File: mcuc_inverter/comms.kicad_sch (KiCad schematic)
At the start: 0 parts

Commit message: Capture bus_sense, temp_sense, comms: all 11 sheets now live
bus_sense: 4x750k + 12.0k string (strict series, 124.5 V/part) into
AMC1311BDWV (pinout verified vs SBAS786C; B-grade 3.0-5.5 V VDD1 is
load-bearing per D022; no input clamp diodes per TI 9.3), HV-side
3.3 V from MCP1804T-3302 (2-28 V in, stocked - no TBV needed) off
the VGD_LS rail, diff-to-SE gain 0.75: V_BUS = 2.988 mV/V, 500 V ->
1.494 V, saturates ~1.50 V, always < 3.3 V.

temp_sense: coldplate NTC channel (B57861S off-board via J1101),
board NTC (NCU18 successor), 6x DNP TS provision pads onto the
module TS pins with D022 rationale quoted on-sheet.

comms: ISO1042DWR isolated CAN (VCC2 pins 11/16 tied - datasheet
requirement), split termination + TVS added (legacy sheet flagged
its own missing protection), USB-C + USBLC6 to MCU 70/71, keyed SWD,
status LEDs, I/O connectors. CAN_TX/RX verified onto MCU pins 96/95;
CONTACTOR_P/N resolve onto the precharge coil driver.

ERC 0 errors; netlist machine-checks per sheet; key cross-sheet
nets independently re-verified. 11 of 11 sheets captured.

Co-Authored-By: Claude Fable 5 <noreply@anthropic.com>
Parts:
- added C1201, C1202: 100nF, Capacitor_SMD:C_0603_1608Metric, symbol Device:C
- added C1203: 4.7nF, Capacitor_SMD:C_0603_1608Metric, symbol Device:C
- added C1204: 4.7uF, Capacitor_SMD:C_0805_2012Metric, symbol Device:C
- added D1201: NUP2105L, Package_TO_SOT_SMD:SOT-23, symbol Power_Protection:NUP2105L
- added D1202: GREEN PWR, LED_SMD:LED_0603_1608Metric, symbol Device:LED
- added D1203: RED FAULT, LED_SMD:LED_0603_1608Metric, symbol Device:LED
- added J1201: CAN bus (H/L/GND/nc), Connector_JST:JST_PH_B4B-PH-K_1x04_P2.00mm_Vertical, symbol Connector_Generic:Conn_01x04
- added J1202: GCT USB4085-GF-A, Connector_USB:USB_C_Receptacle_GCT_USB4085, symbol Connector:USB_C_Receptacle_USB2.0_16P
- added J1203: Aux 12-24 V in, Connector_JST:JST_VH_B2P-VH_1x02_P3.96mm_Vertical, symbol Connector_Generic:Conn_01x02
- added J1204: Main contactor coil, Connector_JST:JST_VH_B4P-VH_1x04_P3.96mm_Vertical, symbol Connector_Generic:Conn_01x04
- added J1205: Hall + motor temp, Connector_JST:JST_SH_SM08B-SRSS-TB_1x08-1MP_P1.00mm_Horizontal, symbol Connector_Generic:Conn_01x08
- added J1206: Encoder / SinCos, Connector_JST:JST_SH_SM08B-SRSS-TB_1x08-1MP_P1.00mm_Horizontal, symbol Connector_Generic:Conn_01x08
- added J1207: Resolver, Connector_JST:JST_SH_SM06B-SRSS-TB_1x06-1MP_P1.00mm_Horizontal, symbol Connector_Generic:Conn_01x06
- added J1208: FTSH-105-01-L-DV-K, Connector_PinHeader_1.27mm:PinHeader_2x05_P1.27mm_Vertical_SMD, symbol Connector:Conn_ARM_JTAG_SWD_10
- added R1202, R1203: 60.4R, Resistor_SMD:R_0603_1608Metric, symbol Device:R
- added R1204, R1205: 5.1k, Resistor_SMD:R_0603_1608Metric, symbol Device:R
- added R1206: 47k, Resistor_SMD:R_0603_1608Metric, symbol Device:R
- added R1207: 22k, Resistor_SMD:R_0603_1608Metric, symbol Device:R
- added R1208, R1209: 1k, Resistor_SMD:R_0603_1608Metric, symbol Device:R
- added U1201: ISO1042DWR, Package_SO:SOIC-16W_7.5x10.3mm_P1.27mm, symbol mcuc:ISO1042DWR
- added U1202: USBLC6-2SC6, Package_TO_SOT_SMD:SOT-23-6, symbol Power_Protection:USBLC6-2SC6
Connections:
- new net: D1203.2 (A), R1209.2
- new net: J1202.A6 (D+), J1202.B6 (D+), U1202.3 (I/O2)
- new net: J1202.A7 (D-), J1202.B7 (D-), U1202.1 (I/O1)
- new net: D1202.2 (A), R1208.2
- new net: C1203.1, R1202.2, R1203.1
- new net +3.3V: C1201.1, J1205.1 (Pin_1), J1206.1 (Pin_1), J1208.1 (VTref), R1208.1, R1209.1, U1201.1 (VCC1)
- new net AUX_IN: J1203.1 (Pin_1)
- new net CANH: D1201.1 (K), J1201.1 (Pin_1), R1202.1, U1201.13 (CANH)
- new net CANL: D1201.2 (K), J1201.2 (Pin_2), R1203.2, U1201.12 (CANL)
- new net CAN_5V: C1202.1, C1204.1, U1201.11 (VCC2), U1201.16 (VCC2)
- new net CAN_GND: C1202.2, C1203.2, C1204.2, D1201.3 (A), J1201.3 (Pin_3), U1201.10 (GND2), U1201.15 (GND2), U1201.9 (GND2)
- new net CAN_RX: U1201.5 (RXD)
- new net CAN_TX: U1201.3 (TXD)
- new net CONTACTOR_N: J1204.2 (Pin_2)
- new net CONTACTOR_P: J1204.1 (Pin_1)
- new net ENC_A_IN: J1206.2 (Pin_2)
- new net ENC_B_IN: J1206.3 (Pin_3)
- new net ENC_I_IN: J1206.4 (Pin_4)
- new net GND: C1201.2, D1202.1 (K), J1202.A1 (GND), J1202.A12 (GND), J1202.B1 (GND), J1202.B12 (GND), J1202.S1 (SHIELD), J1203.2 (Pin_2), J1204.3 (Pin_3), J1205.6 (Pin_6), J1205.7 (Pin_7), J1205.8 (Pin_8), J1206.7 (Pin_7), J1206.8 (Pin_8), J1208.3 (GND), J1208.5 (GND), J1208.9 (GNDDetect), R1204.2, R1205.2, R1207.2, U1201.2 (GND1), U1201.8 (GND1), U1202.2 (GND)
- new net HALL_1_IN: J1205.2 (Pin_2)
- new net HALL_2_IN: J1205.3 (Pin_3)
- new net HALL_3_IN: J1205.4 (Pin_4)
- new net LED_FAULT: D1203.1 (K)
- new net MOTOR_TEMP_IN: J1205.5 (Pin_5)
- new net NRST: J1208.10 (~{RESET})
- new net RES_COS_N: J1207.6 (Pin_6)
- new net RES_COS_P: J1207.5 (Pin_5)
- new net RES_EXC_N: J1207.2 (Pin_2)
- new net RES_EXC_P: J1207.1 (Pin_1)
- new net RES_SIN_N: J1207.4 (Pin_4)
- new net RES_SIN_P: J1207.3 (Pin_3)
- new net SINCOS_COS_IN: J1206.6 (Pin_6)
- new net SINCOS_SIN_IN: J1206.5 (Pin_5)
- new net SWCLK: J1208.4 (SWCLK/TCK)
- new net SWDIO: J1208.2 (SWDIO/TMS)
- new net USB_CC1: J1202.A5 (CC1), R1204.1
- new net USB_CC2: J1202.B5 (CC2), R1205.1
- new net USB_DM: U1202.6 (I/O1)
- new net USB_DP: U1202.4 (I/O2)
- new net USB_VBUS_SENSE: R1206.2, R1207.1
- new net VBUS_DET: J1202.A4 (VBUS), J1202.A9 (VBUS), J1202.B4 (VBUS), J1202.B9 (VBUS), R1206.1, U1202.5 (VBUS)
- no-connect marks 0 -> 11
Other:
- note added: "5.1k CC pulldowns = UFP (device) role."
- note added: "BOARD CONNECTOR BANK - generic header symbols; final connector P/Ns in the BOM (JST families as placeholders)."
- note added: "C1201 at U1201 pin 1."
- note added: "CONTACTOR_P/N: coil pair driven on the precharge sheet (+12 V feed, low-side switch + flyback there). Pin 4 spare. Precharge relay K401 is ON-BOARD (precharge sheet) - its coil needs no connector."
- note added: "Communications and connectors"
- note added: "Dual-line CAN TVS, 24 V working (NUP2105L-class [TBV], SZNUP2105LT1G)."
- note added: "Halls are open-collector with 3.3 V pull-ups on the position sheet (PALTA precedent) - connector supplies +3.3 V + GND."
- note added: "ISOLATED CAN: CAN_5V/CAN_GND come from the aux sheet's NXE2S0505MC (3 kVDC, functional isolation; reinforced barrier budget sits in the HV-facing devices). Legacy CAN.sch reverse-polarity FET (2N7002+MBR0540 on the external 5 V feed) dropped - supply is on-board now. TVS added: legacy sheet's own note flags missing overvoltage protection. ISO1042 pinout verified vs TI SLLSF09E: 1 VCC1, 2/8 GND1, 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"
- note added: "PHASE-CURRENT SENSORS: the three HOYS 200-S/SP33 are chassis-mounted on the phase busbars (apertures) and arrive on 5-pin JST PA harnesses (B05B-PASK class). Their transducer symbols live on the current_sense sheet; board-side harness connectors are footprints on those same nets, handled at layout (D021) - deliberately not duplicated as symbols here."
- note added: "SHIELD tied to GND at the receptacle (chassis strategy at layout)."
- note added: "SPEC.md 12/13, DECISIONS.md D020/D022. Isolated CAN (ISO1042DWR), USB-C 2.0 FS device, SWD debug, status LEDs, board connector bank. CAN topology ported from PALTA pcb_design/CAN.sch (ISO1050 -> ISO1042, D022)."
- note added: "SWD debug: Samtec FTSH-105-01-L-DV-K, 10-pin 1.27 mm, standard ARM Cortex debug pinout (SWO/TDI unused)."
- note added: "Split termination (PALTA pattern): 2x 60.4R + 4.7nF to CAN_GND. Fit for END-NODE use only - remove R1202/R1203 when the inverter is mid-bus (BOM option / jumper at assembly)."
- note added: "Status LEDs: green PWR direct from +3.3 V; red FAULT is LOW-SIDE driven - LED_FAULT pulled low lights it (driver assignment on the supervisor/MCU pass)."
- note added: "USB 2.0 FS device (VESC tool). USB is user-accessible: the reinforced barrier is UPSTREAM - the whole control domain is separated from HV by the gate-driver / AMC1311 / HOYS / ISO1042 barriers (SPEC 5, D017/D022) - so no extra isolation here. USBLC6-2SC6 pinout (SOT-23-6): 1 I/O1, 2 GND, 3 I/O2, 4 I/O2, 5 VBUS, 6 I/O1 - verified vs ST datasheet / official KiCad symbol. VBUS sensed only (self-powe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"
- note removed: "Communications"
- note removed: "Placeholder. Requirements: SPEC.md 12, 13"

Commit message: Wire full MCU pin map; add verified PINOUT.md
All 33 remaining signals wired per the citation-verified map (D023):
phase currents PC0/1/2 on VESC triple-simultaneous ADC channels,
V_BUS PC3, temps PA3/PB0/PC4, SinCos PA5/PA6, I_REF PA4/PA7/PB1,
encoder PC6/7/8 (TIM3), halls PD12/13/14, resolver SPI3 PC10/PC11 +
PA15 boot-safe CS + PD0/PD1/PD2 controls, supervisor GPIOs PD3/4/5,
precharge/contactor/discharge PE2/3/4, LED PE0, VBUS sense PC5, PPM
PB6 (TIM4_CH1, VESC convention - repurposed J1206 spare pin).
PA0/1/2 and PB10/11 reserved with on-sheet notes.

AD2S1205 drive validated in-datasheet: VIH 2.0 V @ 5 V supply, so
3.3 V MCU outputs are legal; its 5 V outputs land on FT pins only.

docs/PINOUT.md: complete table with per-row DS8626 Table 7/9
citations, 5V-tolerance column with the analog-mode caveat, and the
D023 reservations - generated against the post-wiring netlist.

ERC 0 errors (warnings down 224 -> 201 as dangling pins connected).
33/33 nets machine-verified U1-pad-to-counterpart; 6 re-verified
independently before commit.

Co-Authored-By: Claude Fable 5 <noreply@anthropic.com>
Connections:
- net GND: no longer J1206.7 (Pin_7)
- new net PPM: J1206.7 (Pin_7)
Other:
- note added: "J1206 pin 7: PPM (servo) input to MCU PB6/TIM4_CH1 - was the spare position (previously tied to GND)."
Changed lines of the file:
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@@
-	(wire
-		(pts
-			(xy 330.2 132.08) (xy 327.66 132.08)
-		)
-		(stroke
-			(width 0)
-			(type default)
-		)
-	)
-	(wire
-		(pts
-			(xy 327.66 132.08) (xy 327.66 134.62)
-		)
-		(stroke
-			(width 0)
-			(type default)
-		)
-	)
 	(wire
 		(pts
@@
 			)
 			(justify left bottom)
+		)
+	)
+	(wire
+		(pts
+			(xy 322.58 132.08) (xy 330.2 132.08)
+		)
+		(stroke
+			(width 0)
+			(type default)
+		)
+	)
+	(hierarchical_label "PPM"
+		(shape output)
+		(at 322.58 132.08 180)
+		(fields_autoplaced yes)
+		(effects
+			(font
+				(size 1.27 1.27)
+			)
+			(justify right)
+		)
+	)
+	(text "J1206 pin 7: PPM (servo) input to MCU PB6/TIM4_CH1 -\nwas the spare position (previously tied to GND)."
+		(exclude_from_sim no)
+		(at 322.58 143.0 0)
+		(effects
+			(font
+				(size 1.27 1.27)
+			)
+			(justify left bottom)

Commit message: Board-prep: footprint audit complete, HV terminals, off-board flags
474-component audit: 466 valid resolved footprints, 13 off-board
exclusions per D024 (caps to carrier, chassis resistors, HOYS), 4
flagged TBDs (custom flyback + 3 unchosen inductors), zero silent
gaps. Netlist-fatal fixes: Q403 renumbered to Wolfspeed TO-263-7
convention (G1/KS2/S3-7/tab-D8), CSD18543Q3A remapped to KiCad's
SSSGD VSON-8 pairing - both verified in the netlist afterward.

New HV interface terminals J401-J405 (M4 ring-lug pads: DC input,
precharge-R chassis loop, discharge-R return, bus taps) and HOYS
harness headers J501-J503 (JST 2mm; PA-vs-PH footprint flagged TBV)
with net membership machine-verified incl. the OC_TRIP wire-OR and
I_REF paths to the MCU ADCs.

ERC 0 errors, warnings 201 -> 200 (none introduced).

Co-Authored-By: Claude Fable 5 <noreply@anthropic.com>
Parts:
- D1202, D1203: footprint LED_SMD:LED_0603_1608Metric -> LED_SMD:LED_0805_2012Metric
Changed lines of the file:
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@@
 			)
 		)
-		(property "Footprint" "LED_SMD:LED_0603_1608Metric"
+		(property "Footprint" "LED_SMD:LED_0805_2012Metric"
 			(at 109.22 190.5 0)
 			(effects
@@
 			)
 		)
-		(property "Footprint" "LED_SMD:LED_0603_1608Metric"
+		(property "Footprint" "LED_SMD:LED_0805_2012Metric"
 			(at 109.22 198.12 0)
 			(effects

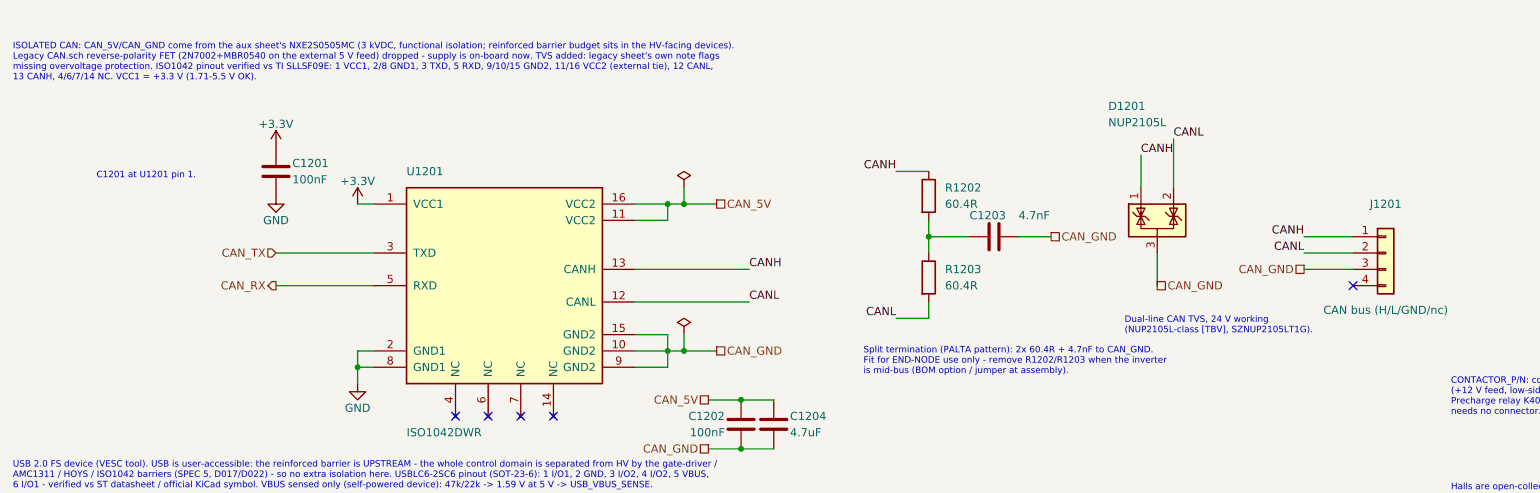
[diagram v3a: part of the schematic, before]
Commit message: Fix precharge, current sense, position, comms per review
Also repairs a library-breaking defect the agent found while working:
the VOM1271T symbol contained a raw newline inside a quoted string,
which silently truncated mcuc_inverter.kicad_sym at parse - every
symbol defined after it was unresolvable. That had been latent since
the symbol was written.

MJ-2/3 - the comparators were wrong twice over: TLV7032 is push-pull
(six of them wire-ORed together plus three open-drain transducer OCD
pins is direct contention), and LM2903's input common-mode range on
3.3 V stops at 1.8 V, below the 2.34 V upper threshold, so the
over-current half could never trip. Now TLV7022DDFR: true open-drain,
rail-to-rail input, 260 ns instead of ~3 us.

MJ-4 - the trip point was really 245-356 A because the thresholds
rode a +-4% rail while the transducer's reference is absolute. Each
phase's window is now servo'd off its own Uref through an OPA376
buffer, so the threshold tracks the sensor: 300 A +-8 A.

MJ-7 - a harness disconnect was not fail-safe: that phase's OCD left
the wire-OR and the input floated. 100k pull-downs make an open
harness read as a large negative current and latch the trip at
power-up, before HV is applied.

MJ-12 - the active discharge can no longer be commanded into a live
bus: SN74LVC1G97 computes DISCHARGE_EN AND NOT(CONTACTOR_EN)
self-contained on the sheet, plus a 10k boot pull-down.

Discharge gate now has a real Miller clamp (BSS138 + 1n + 10k) firing
at V_GS ~1.34 V, below the FET's 1.8 V threshold, in under 15 ns -
the 450 V dv/dt step could previously inject ~4.4 V against a 10M
pull-down and a uA-class photovoltaic turn-off.

Bleeder 18.7k -> 14k (56 k total, 56.4 s to 60 V, meeting the <60 s
requirement it was failing at 75.4 s). Precharge resistor respec'd to
>=65 J. Coil freewheels upsized to ES1G/ES2G with anti-series SMBJ24A
TVS for fast relay release, which forced the coil drivers to 60 V
parts - documented with a 17% margin note.

Position: SinCos f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
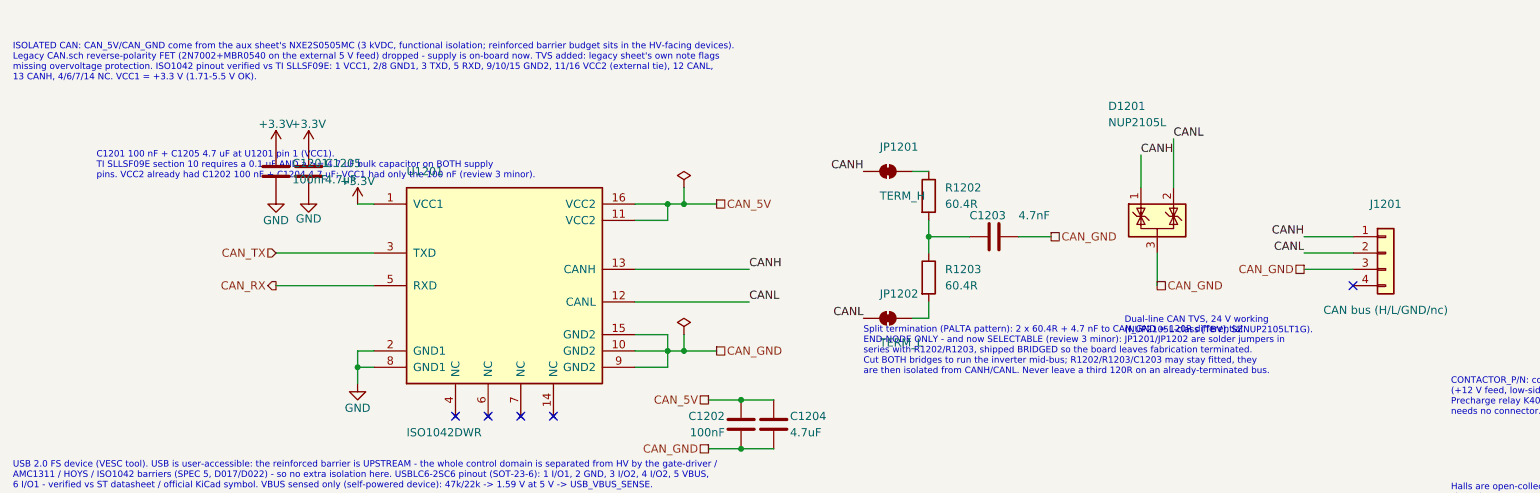
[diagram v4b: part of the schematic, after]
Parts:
- added C1205: 4.7uF, Capacitor_SMD:C_0805_2012Metric, symbol Device:C
- added JP1201: TERM_H, Jumper:SolderJumper-2_P1.3mm_Bridged_RoundedPad1.0x1.5mm, symbol Jumper:SolderJumper_2_Bridged
- added JP1202: TERM_L, Jumper:SolderJumper-2_P1.3mm_Bridged_RoundedPad1.0x1.5mm, symbol Jumper:SolderJumper_2_Bridged
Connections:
- net +3.3V: now also C1205.1
- net CANH: now also JP1201.1 (A); no longer R1202.1
- net CANL: now also JP1202.1 (A); no longer R1203.2
- net GND: now also C1205.2
- new net: JP1201.2 (B), R1202.1
- new net: JP1202.2 (B), R1203.2
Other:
- note added: "C1201 100 nF + C1205 4.7 uF at U1201 pin 1 (VCC1). TI SLLSF09E section 10 requires a 0.1 uF AND a >= 4.7 uF bulk capacitor on BOTH supply pins. VCC2 already had C1202 100 nF + C1204 4.7 uF; VCC1 had only the 100 nF (review 3 minor)."
- note added: "Split termination (PALTA pattern): 2 x 60.4R + 4.7 nF to CAN_GND = 120R differential. END-NODE ONLY - and now SELECTABLE (review 3 minor): JP1201/JP1202 are solder jumpers in series with R1202/R1203, shipped BRIDGED so the board leaves fabrication terminated. Cut BOTH bridges to run the inverter mid-bus; R1202/R1203/C1203 may stay fitted, they are then isolated from CANH/CANL. Never leave a third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"
- note removed: "C1201 at U1201 pin 1."
- note removed: "Split termination (PALTA pattern): 2x 60.4R + 4.7nF to CAN_GND. Fit for END-NODE use only - remove R1202/R1203 when the inverter is mid-bus (BOM option / jumper at assembly)."
